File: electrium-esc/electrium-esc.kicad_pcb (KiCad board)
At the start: 2 copper layers, 187 parts, among them J1 Conn_01x04_Male, J2 USB_MICRO, J3 Conn_01x03_Male, J4 Conn_01x04_Male, J5 Debug Connector, Q1 IRFS7530TRLPBF, Q10 IRFS7530TRLPBF, Q11 IRFS7530TRLPBF, Q12 IRFS7530TRLPBF, Q2 IRFS7530TRLPBF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

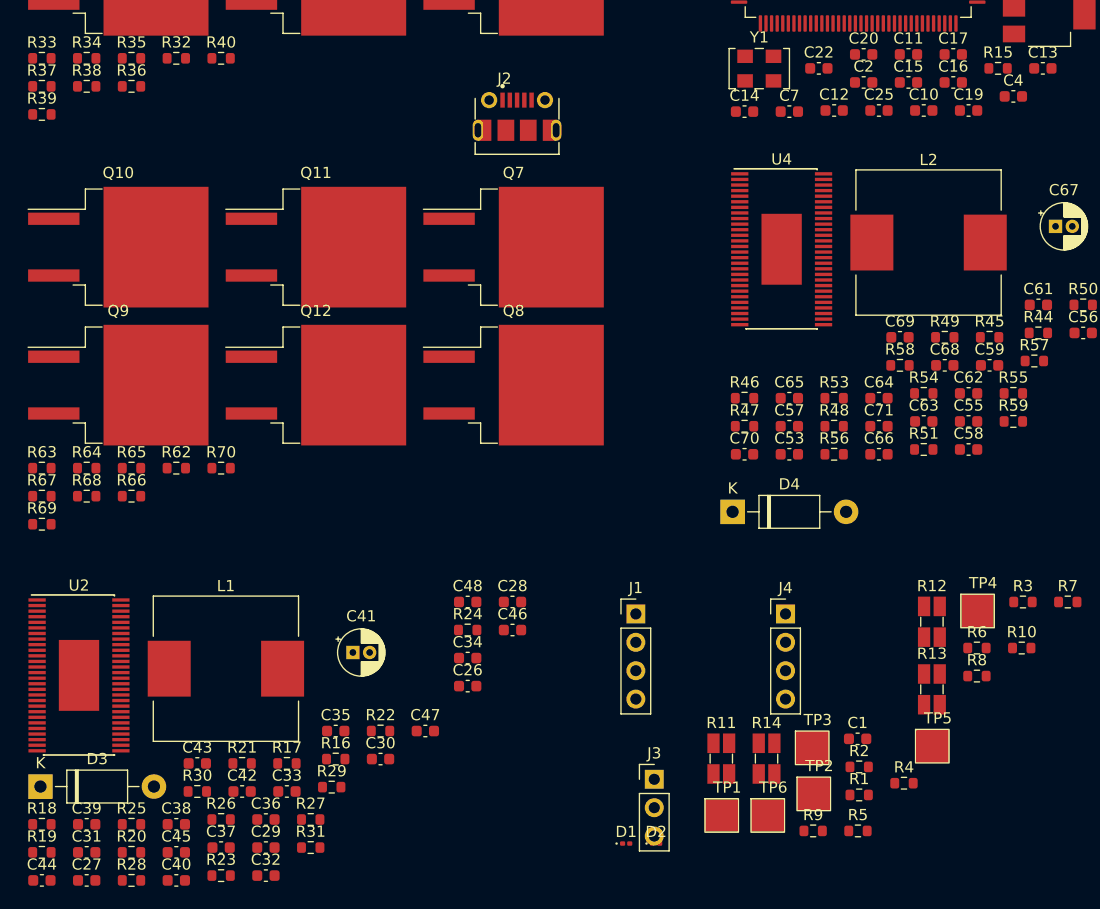
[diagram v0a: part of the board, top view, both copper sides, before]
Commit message: finsihed 1 set of power mosfets
finsihed one set of power mosfets with resistors
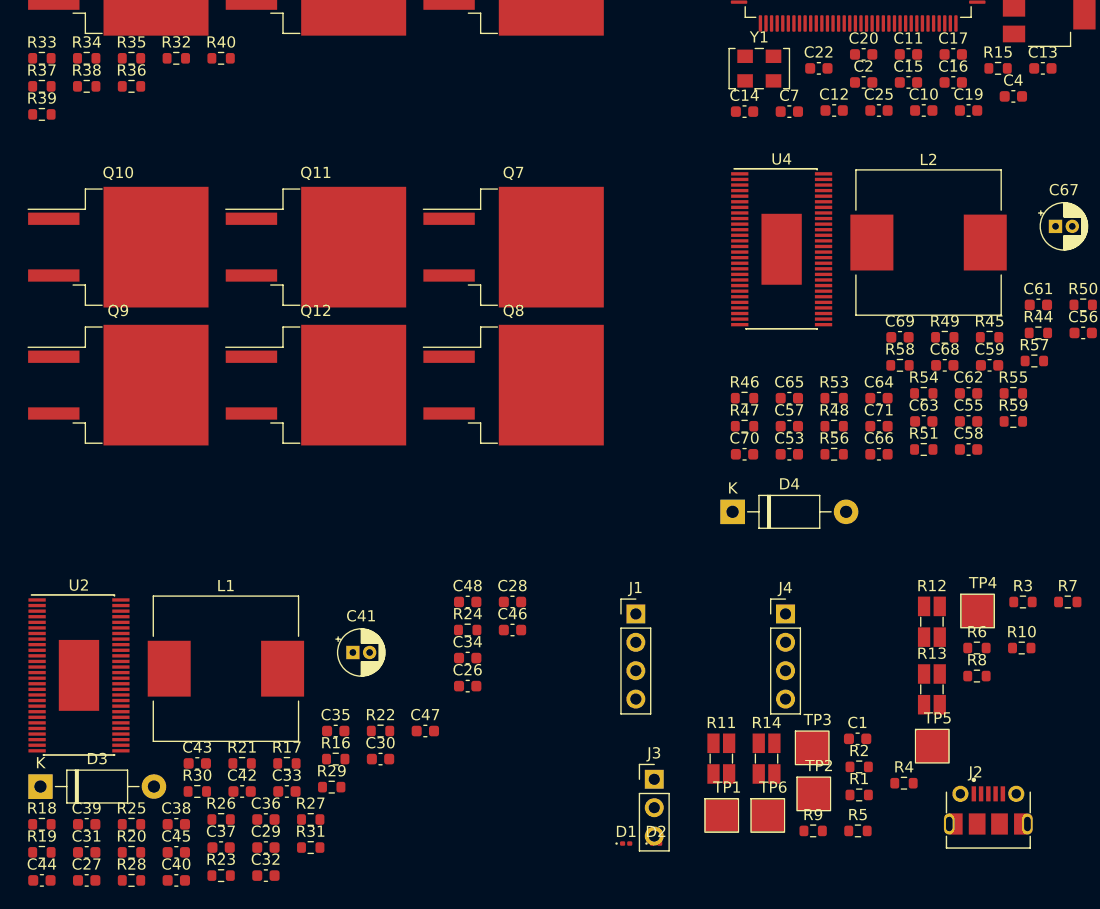
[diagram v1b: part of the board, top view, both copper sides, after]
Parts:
- R62, R63, R64, R65, R66, R67, R68, R69, R70: moved to B.Cu
- moved J2 75.1 mm to (161.6, 129.2)
- moved R63 46.5 mm to (121.9, 86.4), turned to 180 degrees
- moved R64 41.2 mm to (121.9, 94.0), turned to 180 degrees
- moved R62 39.4 mm to (121.9, 76.2), turned to 180 degrees
- moved R68 33.4 mm to (104.1, 76.2), turned to 180 degrees
- moved R69 30.6 mm to (104.1, 88.9), turned to 180 degrees
- moved R67 25.8 mm to (86.4, 76.2), turned to 180 degrees
- moved R66 19.0 mm to (86.4, 81.3), turned to 180 degrees
- moved R70 11.8 mm to (104.1, 94.0), turned to 180 degrees
- moved R65 8.92 mm to (86.4, 88.9), turned to 180 degrees
